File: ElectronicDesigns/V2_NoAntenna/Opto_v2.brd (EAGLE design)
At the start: 27.6 x 14 mm, 7 parts

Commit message: Update gerbers
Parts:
- removed U$1: BGA4C4, LOD_BGA4C40P2X2_84X84X60N:BGA4C40P2X2_84X84X60N
- added U1: TLV1117-18IDCYG3, TLV1117-18IDCYG3:SOT230P700X180-4N
- moved R1 18.6 mm to (21.4, 21.1)
- moved U$2 12.5 mm to (35.3, 10.0), turned to 90 degrees
- moved C1 11.8 mm to (31.2, 11.2), turned to 180 degrees
- moved U$4 11.0 mm to (10.1, 14.8), turned to 270 degrees
- moved C2 7.40 mm to (31.4, 8.76), turned to 180 degrees
- moved U$3 7.32 mm to (26.9, 11.8), turned to 270 degrees
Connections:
- net GND: now also U1.1; no longer U$1.B1, U$1.B2
- net N$1: now also U1.2; no longer U$1.A2
- net N$4: now also U1.3; no longer U$1.A1
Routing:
- net N$1: track 1.85 -> 13.4 mm
- net GND: track 16.7 -> 27.6 mm
- net N$2: track 10.8 -> 15.8 mm
- net IN+: track 22.4 -> 26.5 mm
- net IN-: track 28.2 -> 32.2 mm
- net N$4: track 5.08 -> 7.68 mm
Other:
- board size 27.6 x 14 mm -> 100 x 80 mm
- board text added: "GND"
- board text added: "LED +"

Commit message: Updated gerbers
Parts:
- moved U1 16.4 mm to (45.8, 18.6), turned to 0 degrees
- moved R1 7.47 mm to (28.1, 17.8)
- moved U$2 5.12 mm to (31.8, 13.7), turned to 180 degrees
- moved C1 3.82 mm to (28.4, 13.8)
- moved C2 2.06 mm to (31.9, 10.8)
- moved U$3 1.84 mm to (28.4, 10.8), turned to 0 degrees
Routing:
- net GND: track 27.6 -> 98.0 mm
- net IN-: track 32.2 -> 55.2 mm
- net N$2: track 15.8 -> 38.5 mm
- net IN+: track 26.5 -> 45.7 mm
- net N$4: track 7.68 -> 17.3 mm
- net N$1: track 13.4 -> 14.0 mm
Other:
- board size 100 x 80 mm -> 67.1 x 29 mm

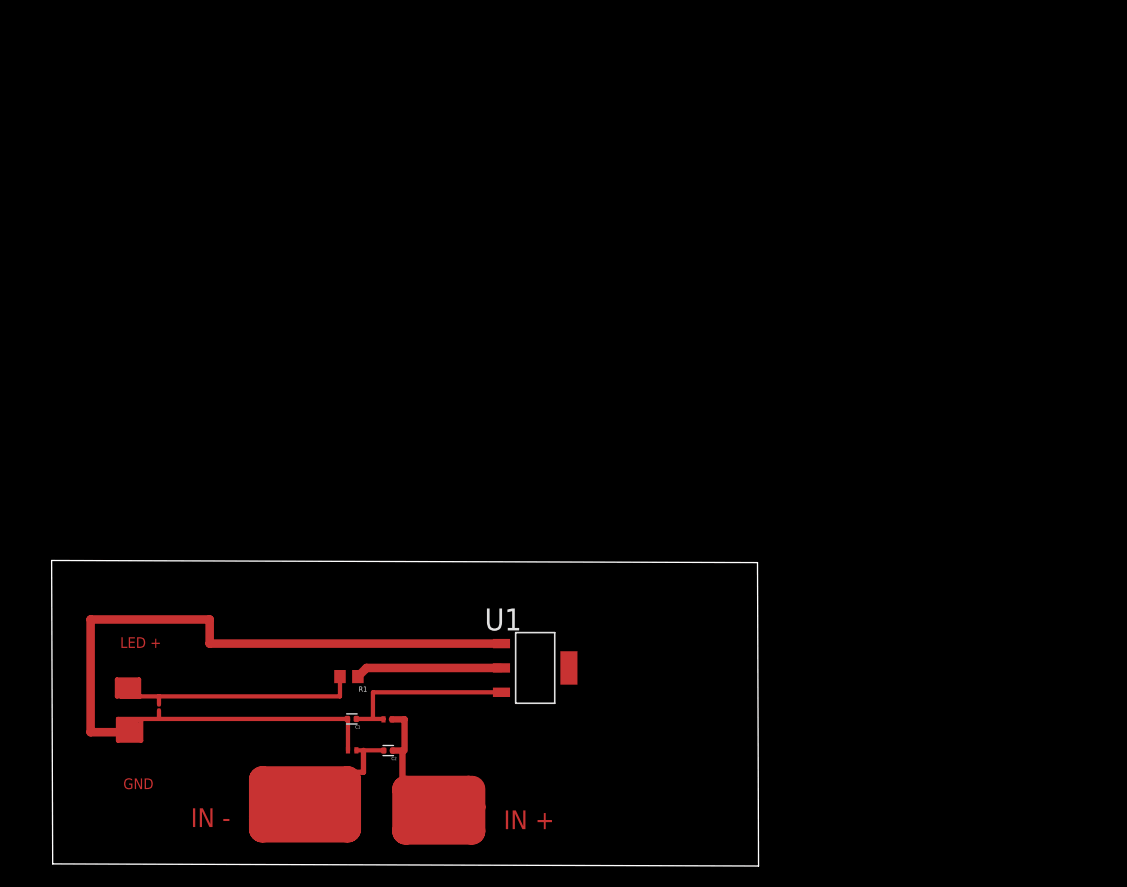
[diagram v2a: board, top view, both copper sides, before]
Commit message: Update PCB Components
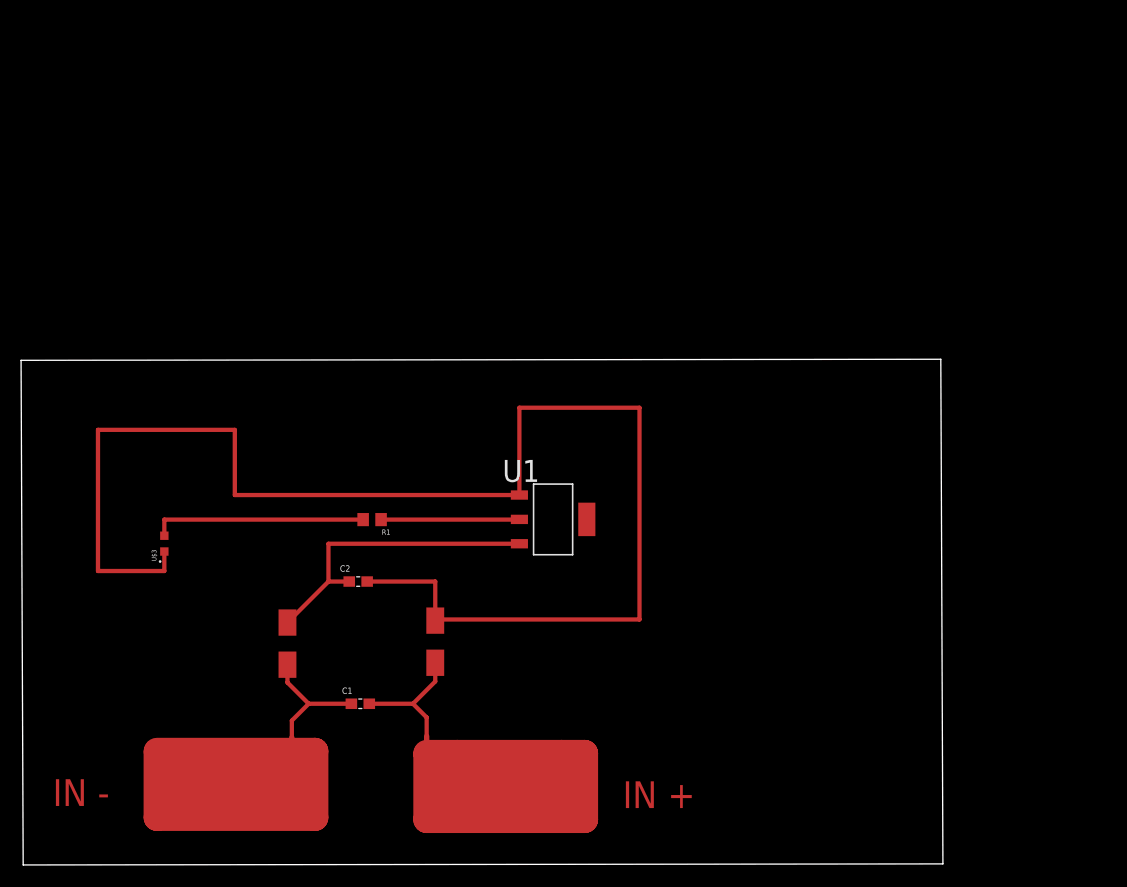
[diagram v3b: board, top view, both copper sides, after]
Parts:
- removed U$4: CREE-TR2227, CREE-TR2227:CREE-TR2227
- added U$1: B220A-13-F, Schottky_0603:SMA-DIODE
- C1, C2: value AMK105BJ225MV-F -> 06036D225KAT2A; device AMK105BJ225MV-F:CAPC1005X55N -> Capacitor_2.2uF_0603:CAPC1608X90
- U$2: value SCHOTTKY0402 -> B220A-13-F; device Schottki_0402:0402_MURATA -> Schottky_0603:SMA-DIODE
- U$3: value SCHOTTKY0402 -> LED; device Schottki_0402:0402_MURATA -> LEDM1608X80:LEDM1608X80
- moved U$3 26.5 mm to (10.6, 30.4), turned to 90 degrees
- moved C2 16.3 mm to (29.0, 26.8), turned to 0 degrees
- moved R1 15.1 mm to (30.3, 32.7)
- moved U1 14.2 mm to (47.5, 32.7)
- moved U$2 8.64 mm to (36.3, 21.1), turned to 270 degrees
- moved C1 1.65 mm to (29.2, 15.2), turned to 0 degrees
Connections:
- net GND: now also C2.2, U$2.1, U$3.C; no longer C1.2, U$3.P$1, U$4.P$2
- net IN+: now also C1.1, U$1.1; no longer C2.1, U$2.P$1
- net IN-: now also C1.2, U$2.2; no longer C2.2, U$3.P$2
- net N$2: now also U$3.A; no longer U$4.P$1
- net N$4: now also C2.1, U$1.2; no longer C1.1, U$2.P$2
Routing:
- net IN+: track 45.7 -> 95.6 mm
- net IN-: track 55.2 -> 95.9 mm
- net GND: track 98.0 -> 137.1 mm
- net N$2: track 38.5 -> 20.4 mm
- net N$4: track 17.3 -> 29.2 mm
- net N$1: track 14.0 -> 13.1 mm
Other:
- board size 67.1 x 29 mm -> 87.5 x 48 mm
- board text removed: "GND"
- board text removed: "LED +"

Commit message: Presentation
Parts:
- removed C2: 06036D225KAT2A, Capacitor_2.2uF_0603:CAPC1608X90
- removed U$2: B220A-13-F, Schottky_0603:SMA-DIODE
- moved U$3 64.2 mm to (74.8, 30.0)
- moved U1 18.8 mm to (28.8, 31.0), turned to 180 degrees
- moved R1 13.8 mm to (44.0, 30.8), turned to 0 degrees
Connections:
- removed net IN-: C1.2, U$2.2
- net GND: now also C1.2; no longer C2.2, U$2.1
- net N$4: no longer C2.1
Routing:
- net IN-: track 95.9 -> 0.00 mm
- net GND: track 137.1 -> 148.3 mm
- net N$2: track 20.4 -> 30.0 mm
- net N$1: track 13.1 -> 11.2 mm
